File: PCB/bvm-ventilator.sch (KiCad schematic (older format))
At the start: 0 parts

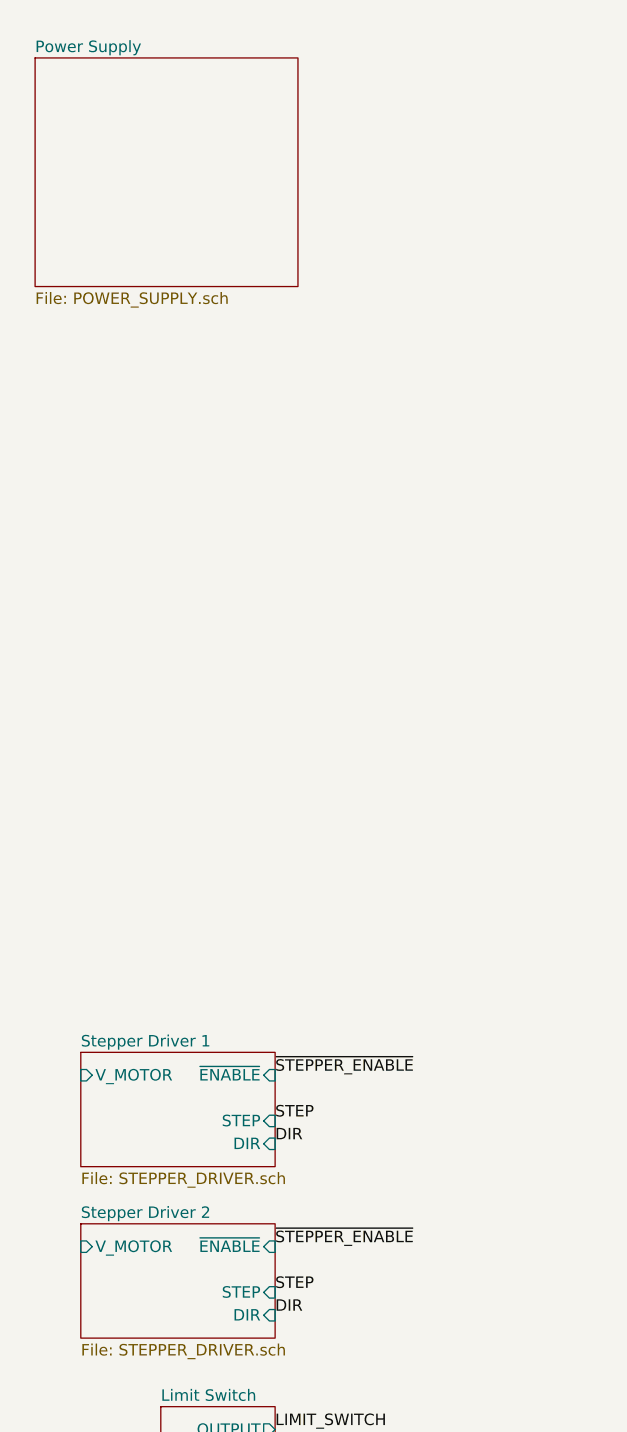
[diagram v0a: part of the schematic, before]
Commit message: Added battery voltage sense
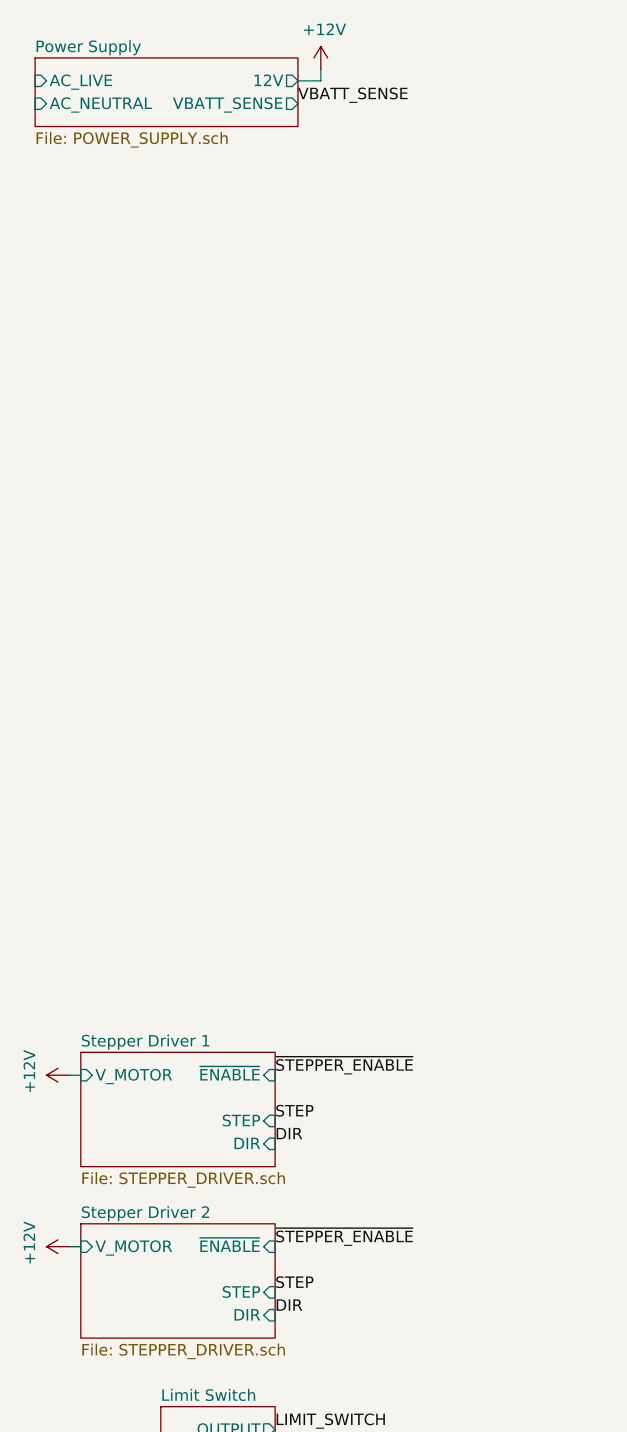
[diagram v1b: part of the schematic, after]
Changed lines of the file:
@@
 $EndSheet
 $Sheet
-S 1150 800  1150 1000
+S 1150 800  1150 300
 U 5E880E11
 F0 "Power Supply" 50
 F1 "POWER_SUPPLY.sch" 50
+F2 "AC_LIVE" I L 1150 900 50
+F3 "AC_NEUTRAL" I L 1150 1000 50
+F4 "12V" O R 2300 900 50
+F5 "VBATT_SENSE" O R 2300 1000 50
 $EndSheet
 $Sheet
@@
 Text Label 6250 3800 0    50   ~ 0
 ~STEPPER_ENABLE
+$Comp
+L power:+12V #PWR?
+U 1 1 5E983996
+P 2400 850
+F 0 "#PWR?" H 2400 700 50  0001 C CNN
+F 1 "+12V" H 2415 1023 50  0000 C CNN
+F 2 "" H 2400 850 50  0001 C CNN
+F 3 "" H 2400 850 50  0001 C CNN
+	1    2400 850
+	1    0    0    -1
+$EndComp
+Wire Wire Line
+	2300 900  2400 900
+Wire Wire Line
+	2400 900  2400 850
+$Comp
+L power:+12V #PWR?
+U 1 1 5E984144
+P 1300 5250
+F 0 "#PWR?" H 1300 5100 50  0001 C CNN
+F 1 "+12V" H 1315 5423 50  0000 C CNN
+F 2 "" H 1300 5250 50  0001 C CNN
+F 3 "" H 1300 5250 50  0001 C CNN
+	1    1300 5250
+	0    -1   -1   0
+$EndComp
+$Comp
+L power:+12V #PWR?
+U 1 1 5E984762
+P 1300 6000
+F 0 "#PWR?" H 1300 5850 50  0001 C CNN
+F 1 "+12V" H 1315 6173 50  0000 C CNN
+F 2 "" H 1300 6000 50  0001 C CNN
+F 3 "" H 1300 6000 50  0001 C CNN
+	1    1300 6000
+	0    -1   -1   0
+$EndComp
+Wire Wire Line
+	1300 5250 1350 5250
+Wire Wire Line
+	1300 6000 1350 6000
+Text Label 2300 1000 0    50   ~ 0
+VBATT_SENSE
 $EndSCHEMATC

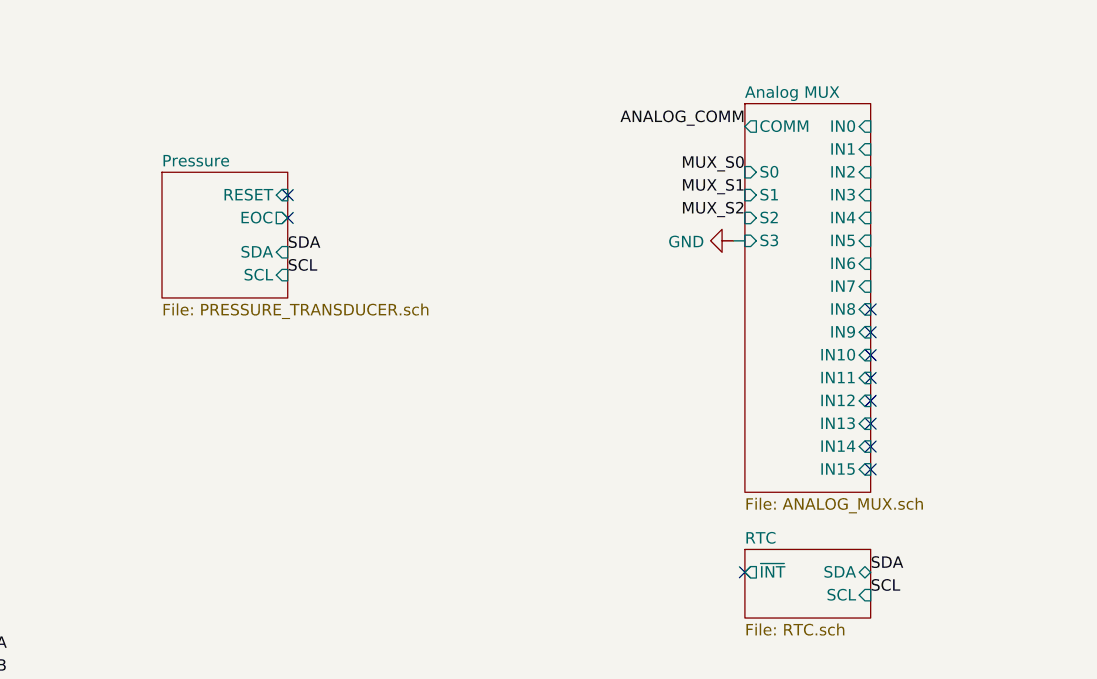
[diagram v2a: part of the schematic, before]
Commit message: Removed Analog MUX
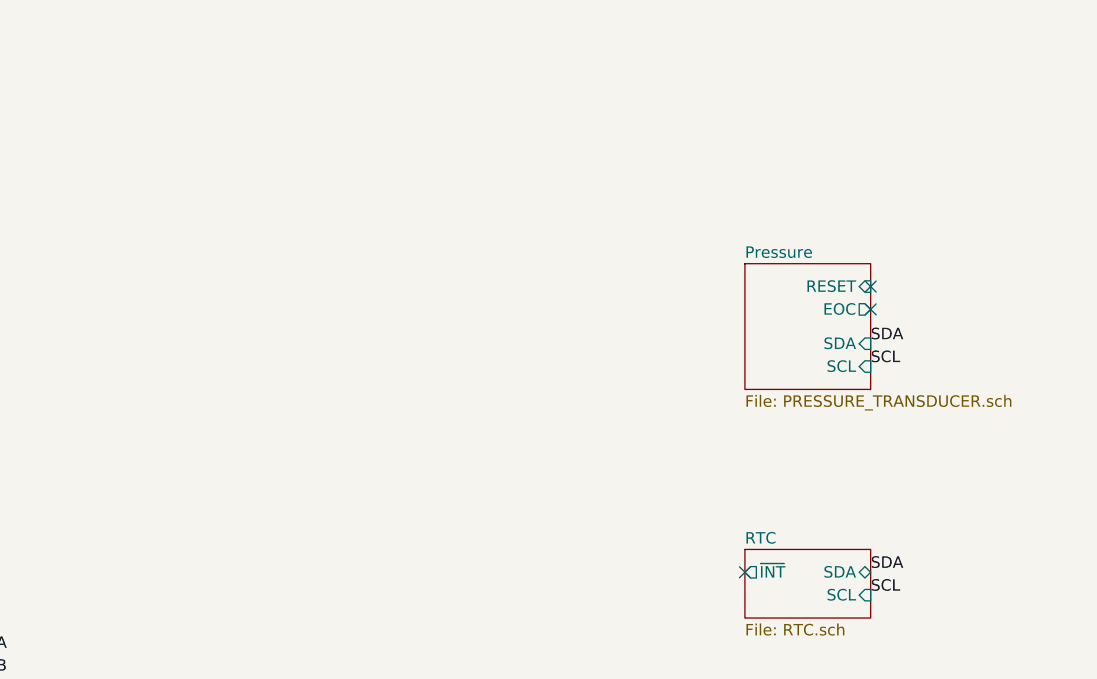
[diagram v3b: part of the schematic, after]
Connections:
- no-connect marks 11 -> 3
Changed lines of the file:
@@
 $Descr A4 11693 8268
 encoding utf-8
-Sheet 1 21
+Sheet 1 20
 Title "BVM Ventilator"
 Date ""
@@
 $EndSheet
 $Sheet
-S 7350 1300 550  550
+S 9900 1700 550  550
 U 5E86C5C8
 F0 "Pressure" 50
 F1 "PRESSURE_TRANSDUCER.sch" 50
-F2 "RESET" I R 7900 1400 50
-F3 "EOC" O R 7900 1500 50
-F4 "SCL" I R 7900 1750 50
-F5 "SDA" I R 7900 1650 50
+F2 "RESET" I R 10450 1800 50
+F3 "EOC" O R 10450 1900 50
+F4 "SCL" I R 10450 2150 50
+F5 "SDA" I R 10450 2050 50
 $EndSheet
-NoConn ~ 7900 1400
-NoConn ~ 7900 1500
+NoConn ~ 10450 1800
+NoConn ~ 10450 1900
 $Sheet
 S 9100 5650 550  200
@@
 Text Label 10450 4000 0    50   ~ 0
 SCL
-Text Label 7900 1650 0    50   ~ 0
+Text Label 10450 2050 0    50   ~ 0
 SDA
-Text Label 7900 1750 0    50   ~ 0
+Text Label 10450 2150 0    50   ~ 0
 SCL
 Text Label 10450 3050 0    50   ~ 0
@@
 VBATT_SENSE
 $Sheet
-S 9900 1000 550  1700
-U 5E8AFDCF
-F0 "Analog MUX" 50
-F1 "ANALOG_MUX.sch" 50
-F2 "IN0" I R 10450 1100 50
-F3 "IN1" I R 10450 1200 50
-F4 "IN2" I R 10450 1300 50
-F5 "IN3" I R 10450 1400 50
-F6 "IN4" I R 10450 1500 50
-F7 "IN5" I R 10450 1600 50
-F8 "IN6" I R 10450 1700 50
-F9 "IN7" I R 10450 1800 50
-F10 "IN8" I R 10450 1900 50
-F11 "IN9" I R 10450 2000 50
-F12 "IN10" I R 10450 2100 50
-F13 "IN11" I R 10450 2200 50
-F14 "IN12" I R 10450 2300 50
-F15 "IN13" I R 10450 2400 50
-F16 "IN14" I R 10450 2500 50
-F17 "IN15" I R 10450 2600 50
-F18 "S0" I L 9900 1300 50
-F19 "S1" I L 9900 1400 50
-F20 "S2" I L 9900 1500 50
-F21 "S3" I L 9900 1600 50
-F22 "COMM" O L 9900 1100 50
-$EndSheet
-Text Label 9900 1100 2    50   ~ 0
-ANALOG_COMM
-$Comp
-L power:GND #PWR?
-U 1 1 5E8B7E49
-P 9850 1600
-F 0 "#PWR?" H 9850 1350 50  0001 C CNN
-F 1 "GND" V 9855 1472 50  0000 R CNN
-F 2 "" H 9850 1600 50  0001 C CNN
-F 3 "" H 9850 1600 50  0001 C CNN
-	1    9850 1600
-	0    1    1    0
-$EndComp
-Wire Wire Line
-	9850 1600 9900 1600
-Text Label 9900 1500 2    50   ~ 0
-MUX_S2
-Text Label 9900 1400 2    50   ~ 0
-MUX_S1
-Text Label 9900 1300 2    50   ~ 0
-MUX_S0
-NoConn ~ 10450 2600
-NoConn ~ 10450 2500
-NoConn ~ 10450 2400
-NoConn ~ 10450 2300
-NoConn ~ 10450 2200
-NoConn ~ 10450 2100
-NoConn ~ 10450 2000
-NoConn ~ 10450 1900
-$Sheet
 S 8100 5000 550  400

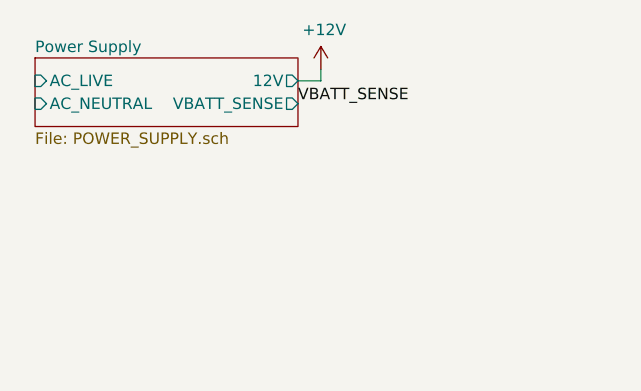
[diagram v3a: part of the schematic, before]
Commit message: Hooked up 3v3 regulator
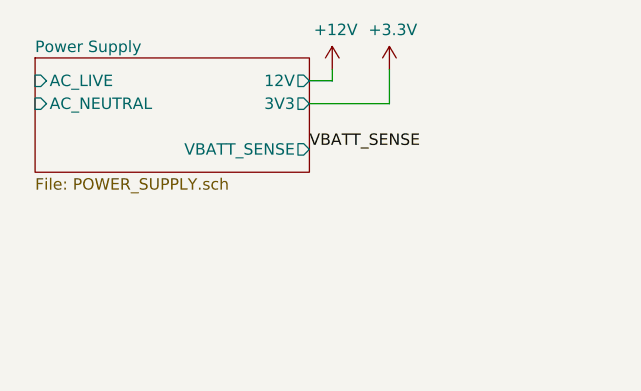
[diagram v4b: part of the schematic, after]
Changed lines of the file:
@@
 $EndSheet
 $Sheet
-S 1150 800  1150 300
+S 1150 800  1200 500
 U 5E880E11
 F0 "Power Supply" 50
@@
 F2 "AC_LIVE" I L 1150 900 50
 F3 "AC_NEUTRAL" I L 1150 1000 50
-F4 "12V" O R 2300 900 50
-F5 "VBATT_SENSE" O R 2300 1000 50
+F4 "12V" O R 2350 900 50
+F5 "VBATT_SENSE" O R 2350 1200 50
+F6 "3V3" O R 2350 1000 50
 $EndSheet
 $Sheet
@@
 L power:+12V #PWR?
 U 1 1 5E983996
-P 2400 850
-F 0 "#PWR?" H 2400 700 50  0001 C CNN
-F 1 "+12V" H 2415 1023 50  0000 C CNN
-F 2 "" H 2400 850 50  0001 C CNN
-F 3 "" H 2400 850 50  0001 C CNN
-	1    2400 850
+P 2450 850
+F 0 "#PWR?" H 2450 700 50  0001 C CNN
+F 1 "+12V" H 2465 1023 50  0000 C CNN
+F 2 "" H 2450 850 50  0001 C CNN
+F 3 "" H 2450 850 50  0001 C CNN
+	1    2450 850
 	1    0    0    -1
 $EndComp
 Wire Wire Line
-	2300 900  2400 900
-Wire Wire Line
-	2400 900  2400 850
+	2350 900  2450 900
+Wire Wire Line
+	2450 900  2450 850
 $Comp
 L power:+12V #PWR?
@@
 Wire Wire Line
 	1300 6000 1350 6000
-Text Label 2300 1000 0    50   ~ 0
+Text Label 2350 1200 0    50   ~ 0
 VBATT_SENSE
+$Comp
+L power:+3.3V #PWR?
+U 1 1 5E8B3135
+P 2700 850
+F 0 "#PWR?" H 2700 700 50  0001 C CNN
+F 1 "+3.3V" H 2715 1023 50  0000 C CNN
+F 2 "" H 2700 850 50  0001 C CNN
+F 3 "" H 2700 850 50  0001 C CNN
+	1    2700 850
+	1    0    0    -1
+$EndComp
+Wire Wire Line
+	2700 850  2700 1000
+Wire Wire Line
+	2700 1000 2350 1000
 $EndSCHEMATC

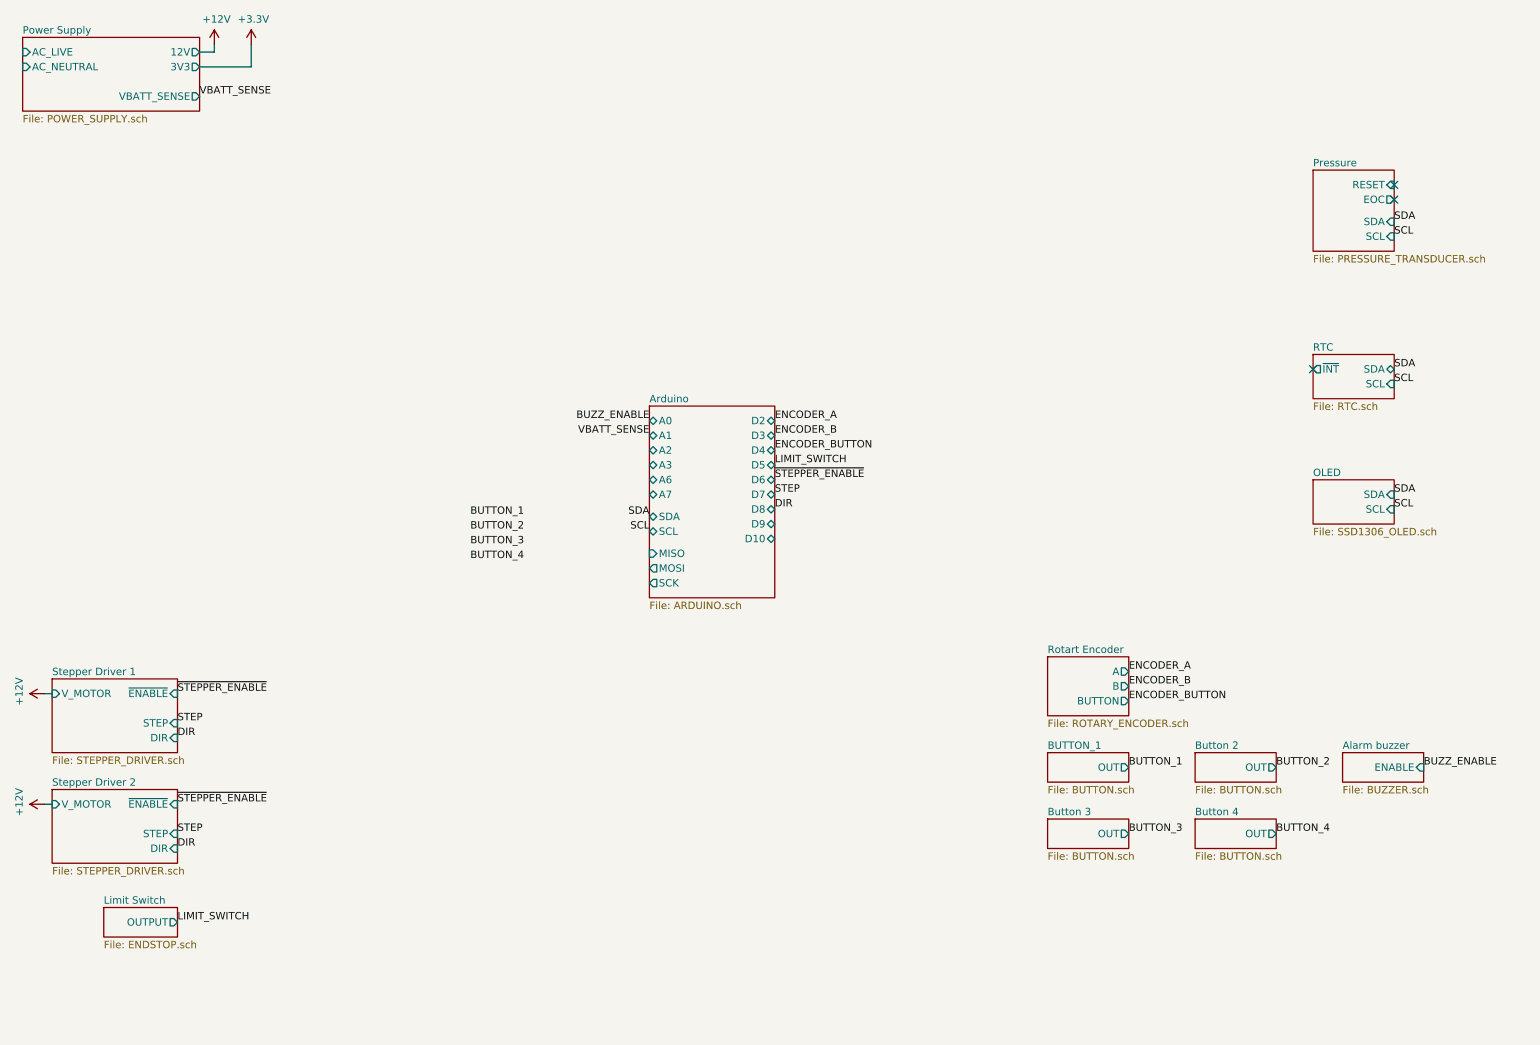
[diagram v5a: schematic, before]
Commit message: Added optical linear encoder
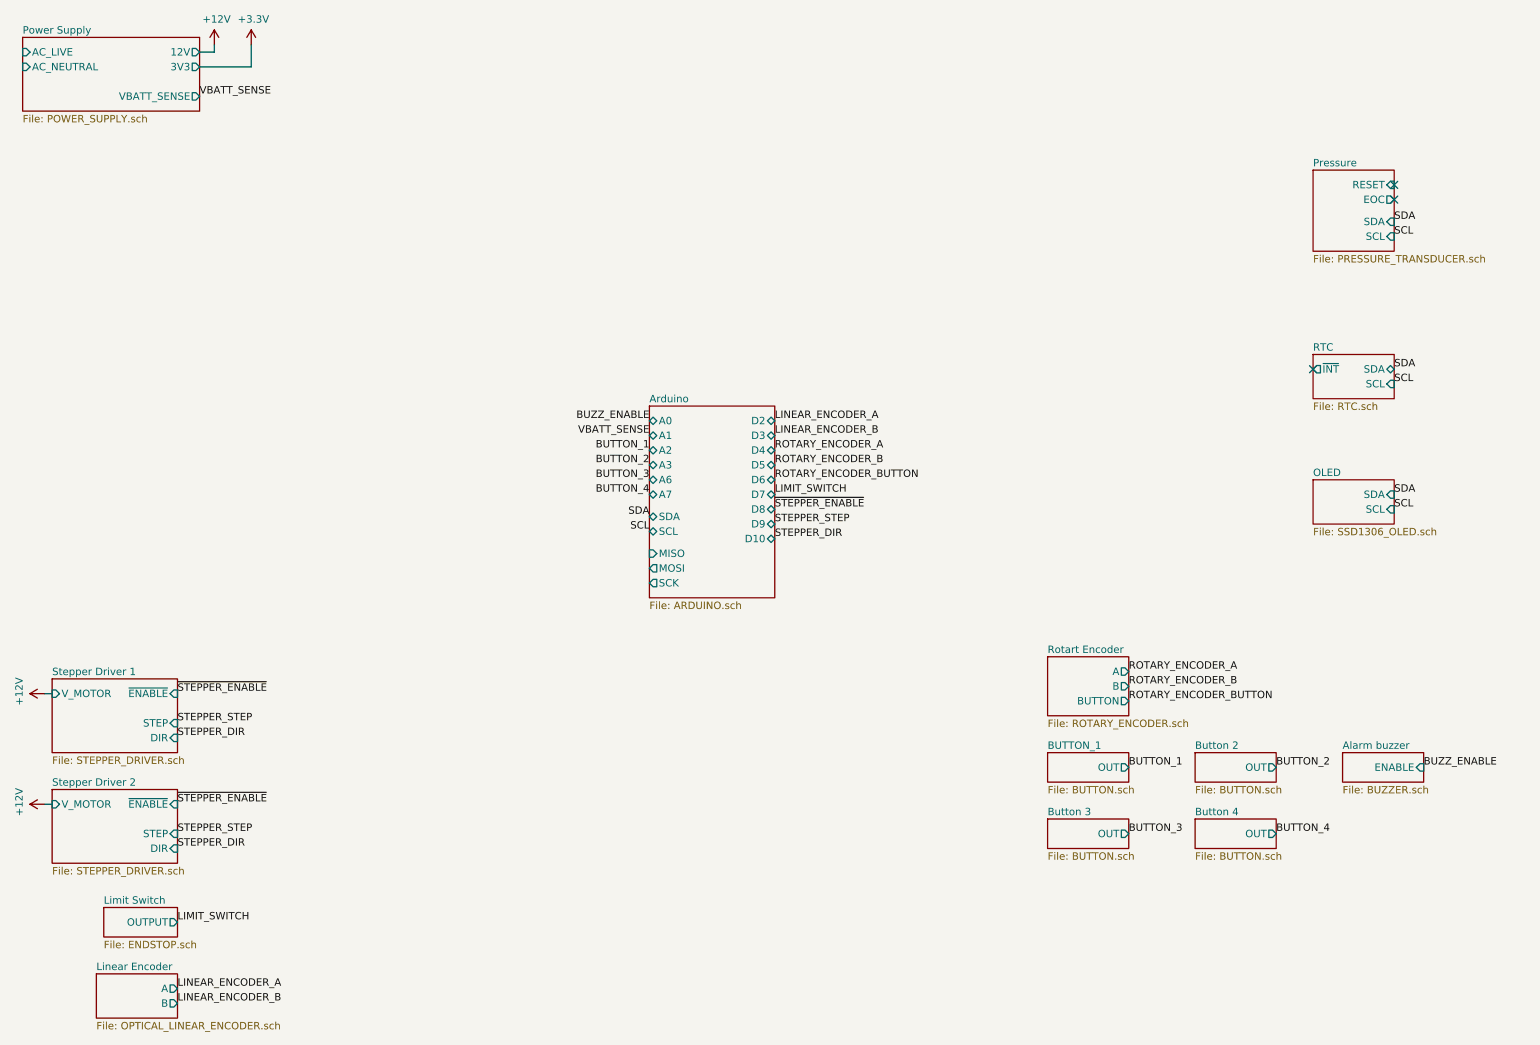
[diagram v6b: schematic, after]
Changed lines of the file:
@@
 $Descr A4 11693 8268
 encoding utf-8
-Sheet 1 20
+Sheet 1 21
 Title "BVM Ventilator"
 Date ""
@@
 SCL
 Text Label 2200 5450 0    50   ~ 0
-STEP
+STEPPER_STEP
 Text Label 2200 5550 0    50   ~ 0
-DIR
+STEPPER_DIR
 Text Label 2200 6200 0    50   ~ 0
-STEP
+STEPPER_STEP
 Text Label 2200 6300 0    50   ~ 0
-DIR
-Text Label 6250 3900 0    50   ~ 0
-STEP
-Text Label 6250 4000 0    50   ~ 0
-DIR
+STEPPER_DIR
+Text Label 6250 4100 0    50   ~ 0
+STEPPER_STEP
+Text Label 6250 4200 0    50   ~ 0
+STEPPER_DIR
 Text Label 10650 5750 0    50   ~ 0
 BUZZ_ENABLE
@@
 BUTTON_2
 NoConn ~ 9900 3050
-Text Label 6250 3700 0    50   ~ 0
+Text Label 6250 3900 0    50   ~ 0
 LIMIT_SWITCH
 Text Label 2200 6800 0    50   ~ 0
@@
 $EndSheet
 Text Label 8650 5100 0    50   ~ 0
-ENCODER_A
+ROTARY_ENCODER_A
 Text Label 8650 5200 0    50   ~ 0
-ENCODER_B
+ROTARY_ENCODER_B
 Text Label 8650 5300 0    50   ~ 0
-ENCODER_BUTTON
-Text Label 6250 3400 0    50   ~ 0
-ENCODER_A
-Text Label 6250 3500 0    50   ~ 0
-ENCODER_B
+ROTARY_ENCODER_BUTTON
 Text Label 6250 3600 0    50   ~ 0
-ENCODER_BUTTON
+ROTARY_ENCODER_A
+Text Label 6250 3700 0    50   ~ 0
+ROTARY_ENCODER_B
+Text Label 6250 3800 0    50   ~ 0
+ROTARY_ENCODER_BUTTON
 $Sheet
 S 8100 5650 550  200
@@
 Text Label 8650 6200 0    50   ~ 0
 BUTTON_3
-Text Label 4550 4050 2    50   ~ 0
+Text Label 5400 3600 2    50   ~ 0
 BUTTON_1
-Text Label 4550 4250 2    50   ~ 0
+Text Label 5400 3800 2    50   ~ 0
 BUTTON_3
-Text Label 4550 4150 2    50   ~ 0
+Text Label 5400 3700 2    50   ~ 0
 BUTTON_2
-Text Label 4550 4350 2    50   ~ 0
+Text Label 5400 3900 2    50   ~ 0
 BUTTON_4
 Text Label 2200 5250 0    50   ~ 0
 ~STEPPER_ENABLE
-Text Label 6250 3800 0    50   ~ 0
+Text Label 6250 4000 0    50   ~ 0
 ~STEPPER_ENABLE
 $Comp
@@
 Wire Wire Line
 	2700 1000 2350 1000
+$Sheet
+S 1650 7150 550  300
+U 5E90196F
+F0 "Linear Encoder" 50
+F1 "OPTICAL_LINEAR_ENCODER.sch" 50
+F2 "A" O R 2200 7250 50
+F3 "B" O R 2200 7350 50
+$EndSheet
+Text Label 2200 7250 0    50   ~ 0
+LINEAR_ENCODER_A
+Text Label 2200 7350 0    50   ~ 0
+LINEAR_ENCODER_B
+Text Label 6250 3400 0    50   ~ 0
+LINEAR_ENCODER_A
+Text Label 6250 3500 0    50   ~ 0
+LINEAR_ENCODER_B
 $EndSCHEMATC
